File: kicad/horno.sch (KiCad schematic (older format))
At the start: 8 parts, among them P10 Alimentación, P2 teclado, P4 TRIAC, P7 Pantalla, P9 fin_carrera, Q1 BC547

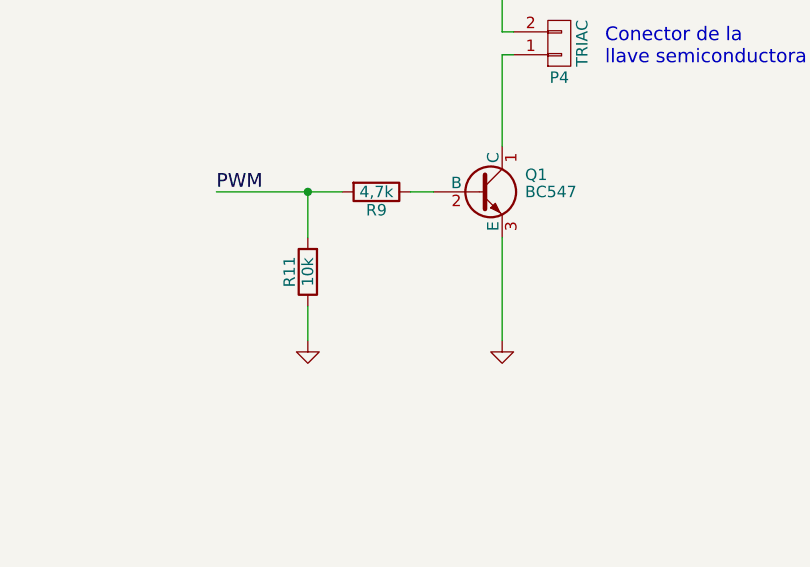
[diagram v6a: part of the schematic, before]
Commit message: agregar LED indicador del PWM.
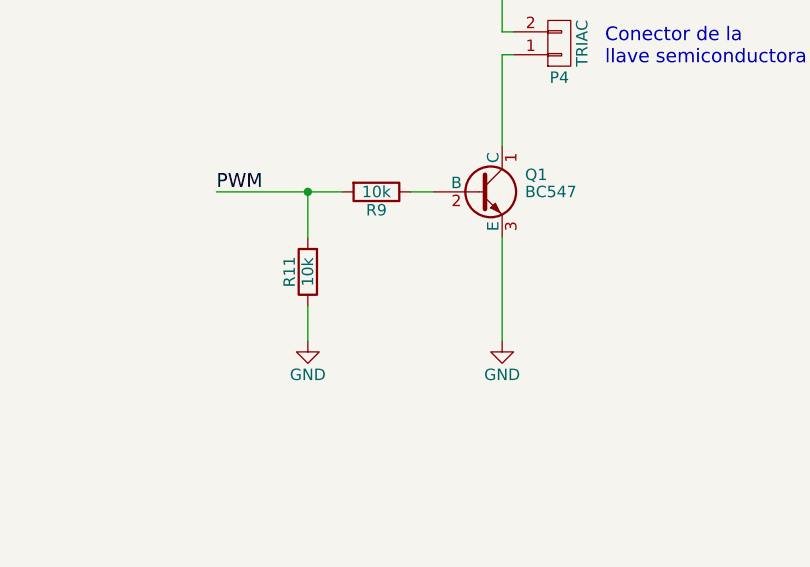
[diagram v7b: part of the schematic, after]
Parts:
- R9: value 4,7k -> 10k
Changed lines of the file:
@@
 P 7400 2350
 F 0 "R9" V 7480 2350 50  0000 C CNN
-F 1 "4,7k" V 7400 2350 50  0000 C CNN
+F 1 "10k" V 7400 2350 50  0000 C CNN
 F 2 "Resistors_ThroughHole:Resistor_Horizontal_RM10mm" V 7330 2350 50  0001 C CNN
 F 3 "" H 7400 2350 50  0000 C CNN
@@
 P 7950 3000
 F 0 "#PWR5" H 7950 2750 50  0001 C CNN
-F 1 "GND" H 7950 2850 50  0001 C CNN
+F 1 "GND" H 7950 2850 50  0000 C CNN
 F 2 "" H 7950 3000 50  0000 C CNN
 F 3 "" H 7950 3000 50  0000 C CNN
@@
 P 7100 3000
 F 0 "#PWR3" H 7100 2750 50  0001 C CNN
-F 1 "GND" H 7100 2850 50  0001 C CNN
+F 1 "GND" H 7100 2850 50  0000 C CNN
 F 2 "" H 7100 3000 50  0000 C CNN
 F 3 "" H 7100 3000 50  0000 C CNN
